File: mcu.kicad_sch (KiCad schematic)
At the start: 59 parts, among them J10 Micro_SD_Card, J11 Conn_01x06, J12 Conn_01x02, J14 USB_B, J8 Conn_02x05_Odd_Even, SW1 SW_Push, SW2 SW_Push, U24 REF3333, U25 LPS25HB, U26 STM32F427ZGTx, U27 USBLC6-2SC6, Y1 8MHz

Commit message: Several optimizations
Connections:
- net DIGITAL5: now reaches U26.66 (PE13)
- net DIGITAL6: now reaches U26.68 (PE15)
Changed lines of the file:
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@@
+    (effects (font (size 1.27 1.27)) (justify right))
+  )
+  (hierarchical_label "DIGITAL6" (shape input) (at 104.14 243.205 180) (fields_autoplaced)
     (effects (font (size 1.27 1.27)) (justify right))
   )
@@
     (effects (font (size 1.27 1.27)) (justify left))
   )
+  (hierarchical_label "DIGITAL5" (shape input) (at 104.14 238.125 180) (fields_autoplaced)
+    (effects (font (size 1.27 1.27)) (justify right))
+  )
   (symbol (lib_id "MCU_ST_STM32F7:STM32F767ZITx") (at 134.62 159.385 0) (unit 1)

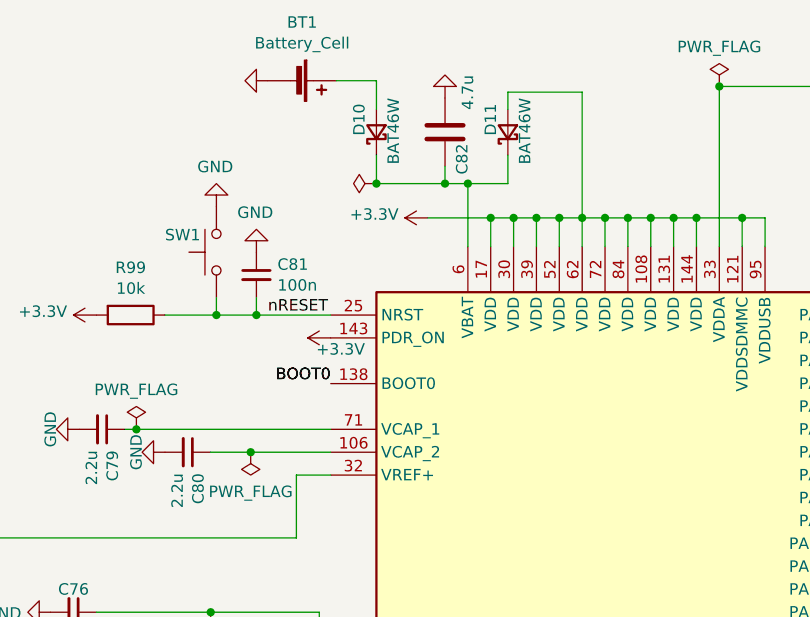
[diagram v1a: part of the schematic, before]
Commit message: Fix connector, optimize psu
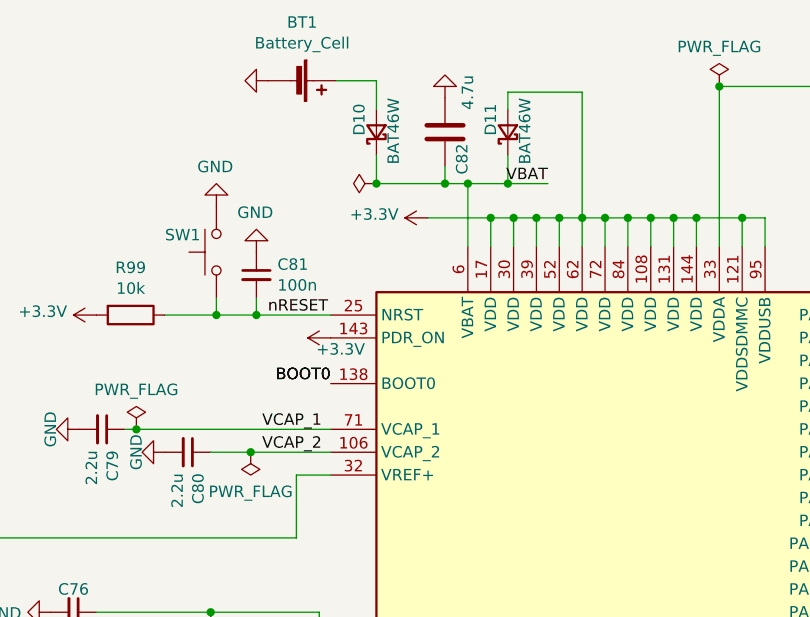
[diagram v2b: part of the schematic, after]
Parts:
- D17: LCSC C8678 -> C15874
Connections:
- net VCAP_2: now reaches C80.1, U26.106 (VCAP_2)
- net VBAT: now reaches C82.1, D10.1 (K), D11.1 (K), U26.6 (VBAT)
- net VCAP_1: now reaches C79.1, U26.71 (VCAP_1)
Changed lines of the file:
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@@
   (junction (at 134.62 252.73) (diameter 0) (color 0 0 0 0)
   )
+  (junction (at 123.825 60.96) (diameter 0) (color 0 0 0 0)
+  )
   (junction (at 65.405 260.35) (diameter 0) (color 0 0 0 0)
   )
@@
     (stroke (width 0) (type default))
   )
+  (wire (pts (xy 123.825 60.96) (xy 128.27 60.96))
+    (stroke (width 0) (type default))
+  )
   (wire (pts (xy 55.245 100.33) (xy 55.245 102.235))
     (stroke (width 0) (type default))
@@
     (effects (font (size 1.27 1.27)) (justify right bottom))
   )
+  (label "VCAP_2" (at 96.52 90.805 0) (fields_autoplaced)
+    (effects (font (size 1.27 1.27)) (justify left bottom))
+  )
   (label "LED3" (at 104.14 217.805 180) (fields_autoplaced)
     (effects (font (size 1.27 1.27)) (justify right bottom))
@@
     (effects (font (size 1.27 1.27)) (justify left bottom))
   )
+  (label "VBAT" (at 128.27 60.96 180) (fields_autoplaced)
+    (effects (font (size 1.27 1.27)) (justify right bottom))
+  )
   (label "AUX_SPI_SCK" (at 81.28 179.705 0) (fields_autoplaced)
     (effects (font (size 1.27 1.27)) (justify left bottom))
@@
     (effects (font (size 1.27 1.27)) (justify right bottom))
   )
+  (label "VCAP_1" (at 96.52 88.265 0) (fields_autoplaced)
+    (effects (font (size 1.27 1.27)) (justify left bottom))
+  )
   (label "AUX_SPI_MISO" (at 292.735 226.695 0) (fields_autoplaced)
     (effects (font (size 1.27 1.27)) (justify left bottom))
@@
       (effects (font (size 1.27 1.27)) hide)
     )
-    (property "LCSC" "C8678" (at 276.225 78.105 0)
+    (property "LCSC" "C15874" (at 276.225 78.105 0)
       (effects (font (size 1.27 1.27)) hide)
     )

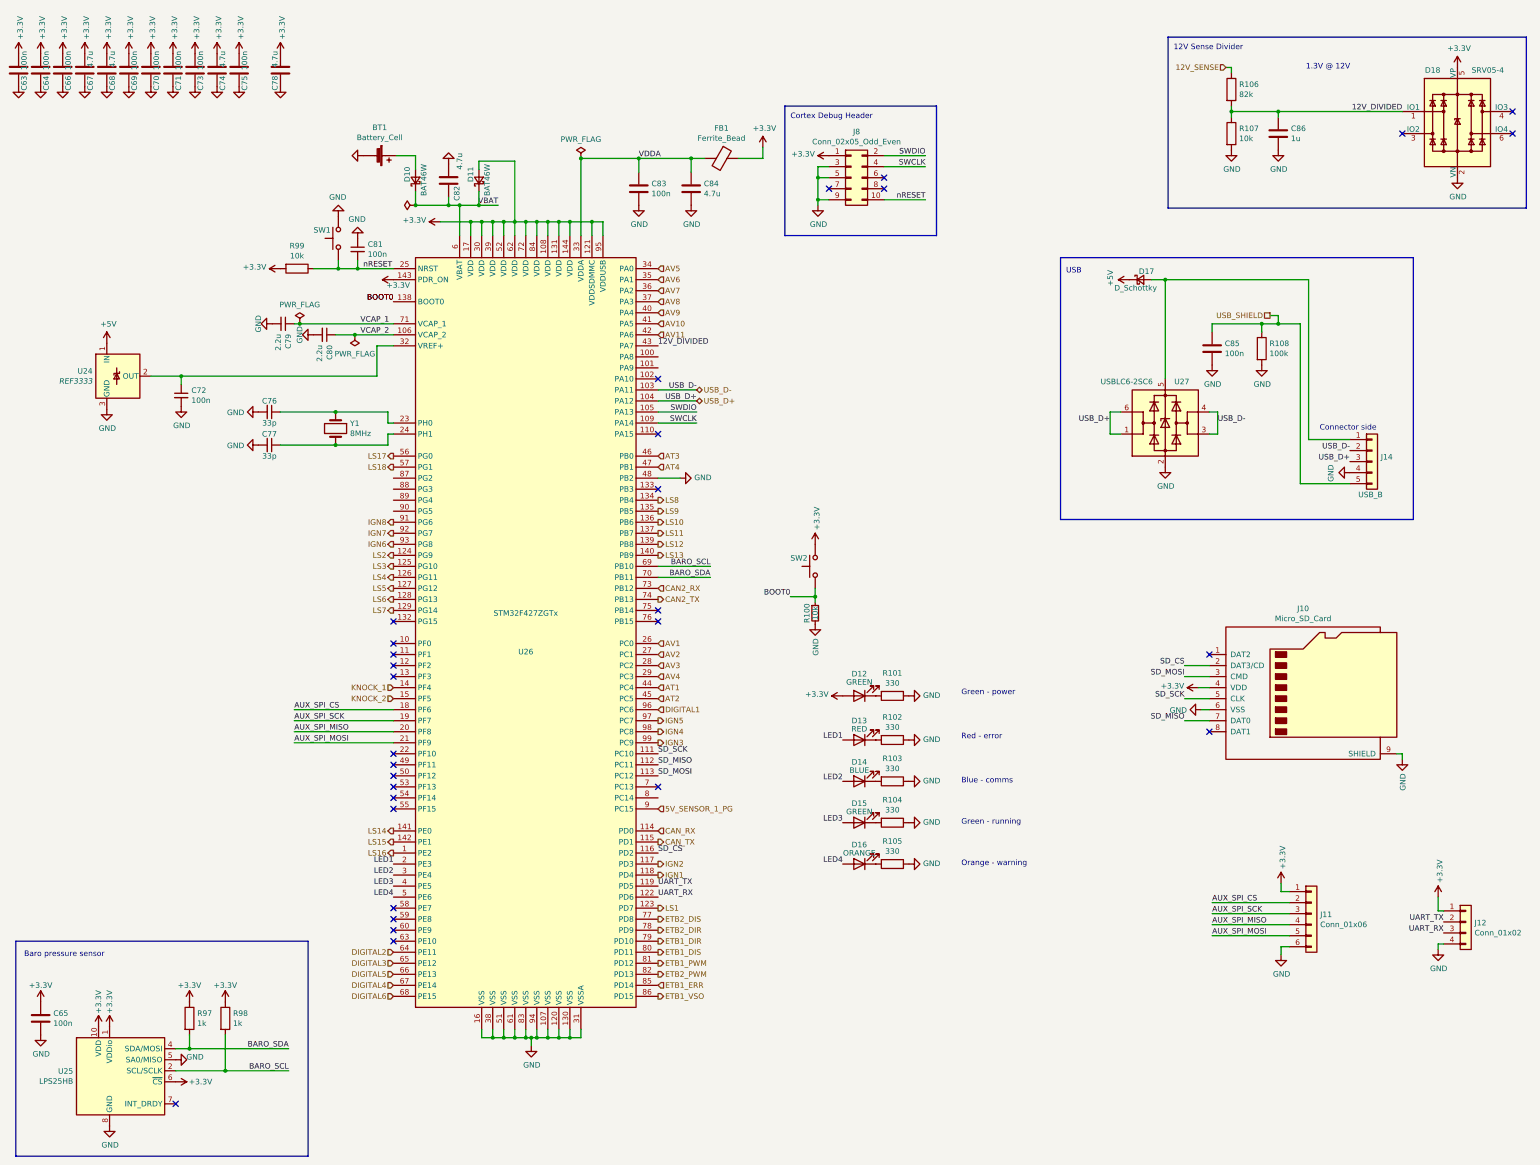
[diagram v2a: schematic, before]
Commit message: Add Stepper, fix Connector, add Testpoints, several changes
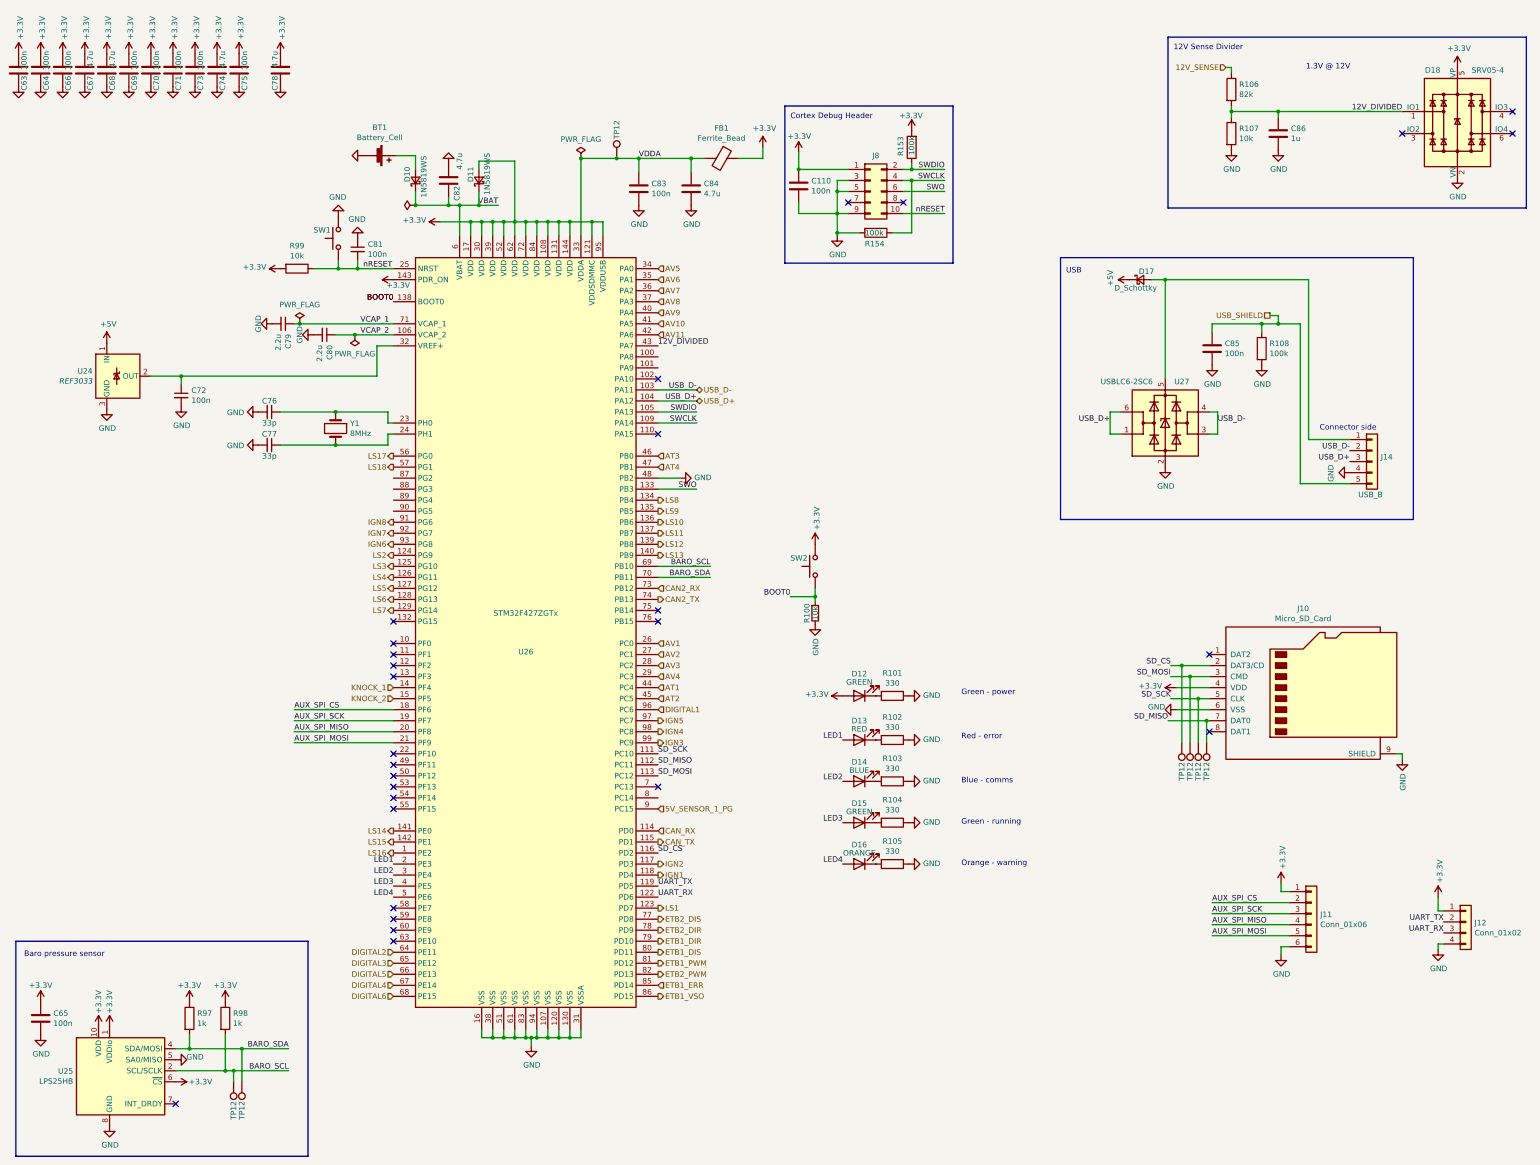
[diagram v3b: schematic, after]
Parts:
- added C110: 100n, Capacitor_SMD:C_0603_1608Metric, symbol Device:C
- added R153, R154: 100k, Resistor_SMD:R_0402_1005Metric, symbol Device:R
- added TP12 (x7): TestPoint, TestPoint:TestPoint_Pad_D1.0mm, symbol Connector:TestPoint
- D10, D11: value BAT46W -> 1N5819WS; footprint Diode_SMD:D_SOD-123 -> Diode_SMD:D_SOD-323; LCSC C83152 -> C191023
- D13: LCSC C84263 -> C2286
- D17: LCSC C15874 -> C14996
- J11, J12, J8: now left out of the parts list
- R97, R98: LCSC C106235 -> C11702
- SW1, SW2: LCSC C318887 -> C318884
- U24: value REF3333 -> REF3033; LCSC C130016 -> C36658; PN REF3033 -> (none)
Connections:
- net +3V3: now also C110.1, R153.2
- net BARO_SCL: now also TP12.1
- net BARO_SDA: now also TP12.1
- net GND: now also C110.2, R154.2
- net SD_CS: now also TP12.1
- net SD_MISO: now also TP12.1
- net SD_MOSI: now also TP12.1
- net SD_SCK: now also TP12.1
- net SWCLK: now also R154.1
- net SWDIO: now also R153.1
- net VDDA: now also TP12.1
- net SWO: now reaches U26.133 (PB3)
- net SWO: now also J8.6 (Pin_6)
- no-connect marks 30 -> 28
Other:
- moved on the sheet: J8

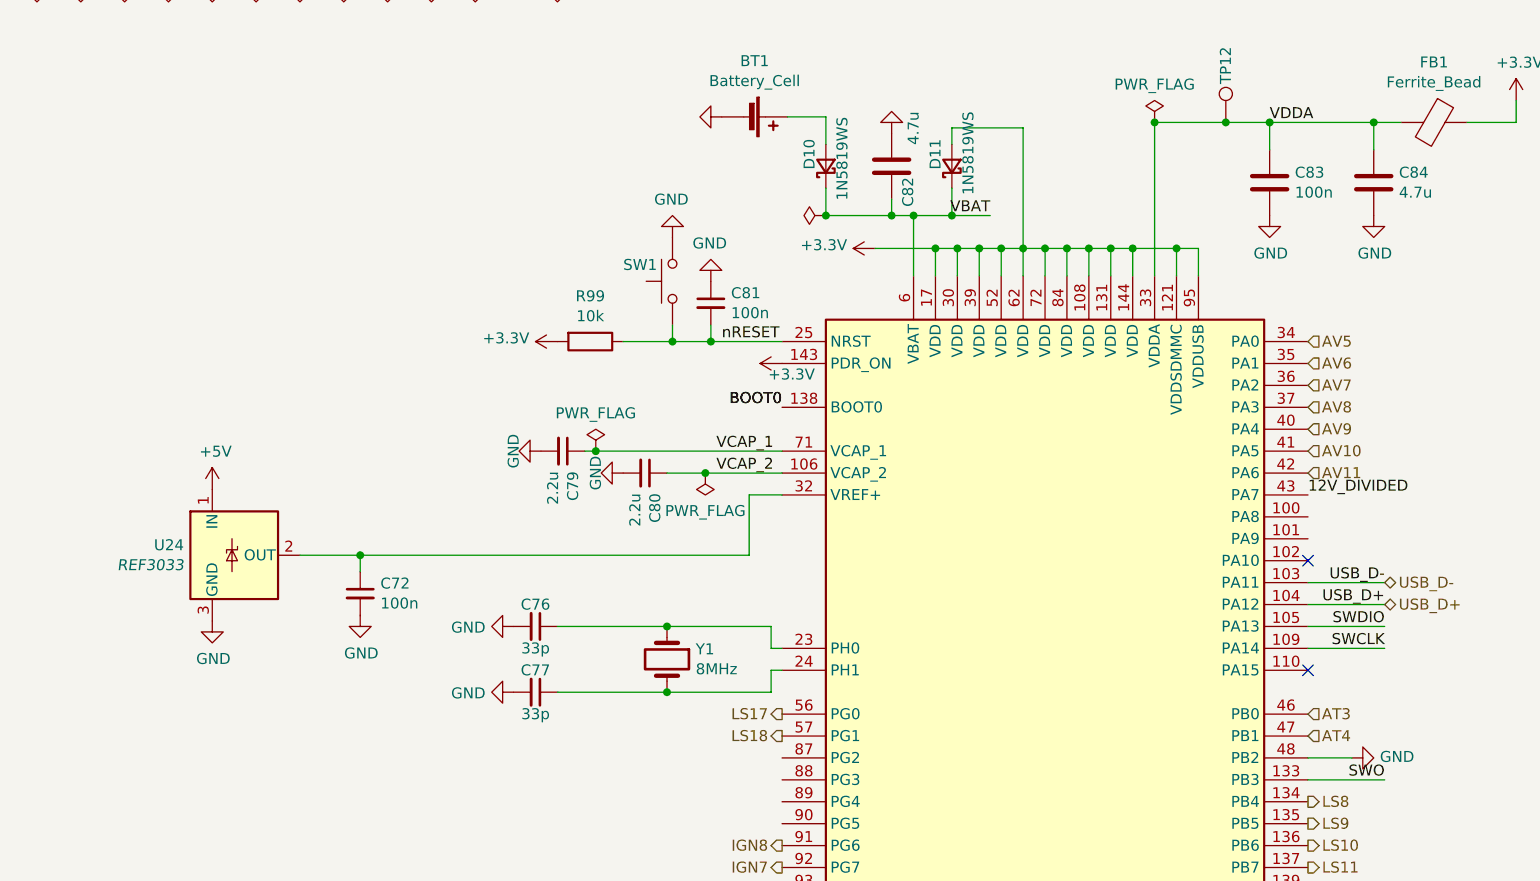
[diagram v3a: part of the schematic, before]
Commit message: Production optimizations, voltage superv, etb sv conn
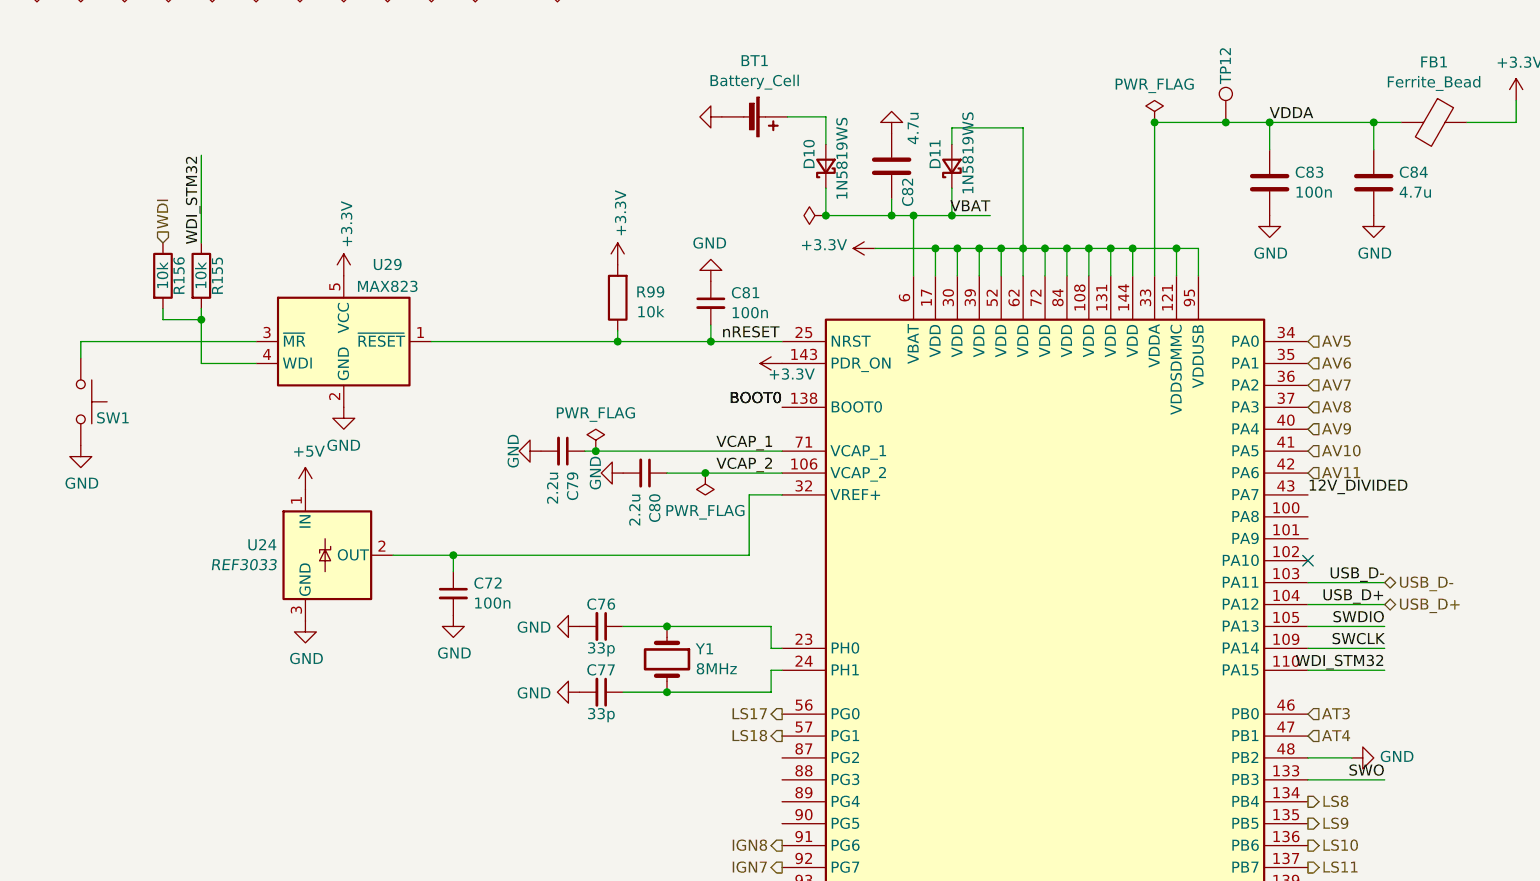
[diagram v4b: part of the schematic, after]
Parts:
- added R155, R156: 10k, Resistor_SMD:R_0402_1005Metric, symbol Device:R
- added U29: MAX823, Package_TO_SOT_SMD:SOT-23-5, symbol MAX823:MAX823
- BT1, J10: JLCRotOffset (none) -> 180
- J14: JLCPosOffset (none) -> -1.27,-2.1
- U27: JLCRotOffset (none) -> 90
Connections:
- net +3V3: now also U29.5 (VCC)
- net GND: now also U29.2 (GND)
- net nRESET: now also U29.1 (~{RESET}); no longer SW1.1
- net WDI_STM32: now reaches U26.110 (PA15)
- net WDI_STM32: now also R155.1
- new net: SW1.1, U29.3 (~{MR})
- new net: R155.2, R156.2, U29.4 (WDI)
- new net WDI: R156.1
- no-connect marks 28 -> 27
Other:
- moved on the sheet: C72, C76, C77, R99, SW1, U24

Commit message: Optimize
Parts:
- added JP5: Jumper_2_Bridged, Jumper:SolderJumper-2_P1.3mm_Open_RoundedPad1.0x1.5mm, symbol Jumper:SolderJumper_2_Open
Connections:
- net ETB1_VSO: now also JP5.1 (A); no longer U26.86 (PD15)
- net SRV05-4-IO2: now reaches D18.3 (IO2)
- new net: JP5.2 (B), U26.86 (PD15)
- no-connect marks 27 -> 26
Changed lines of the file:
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@@
   (no_connect (at 208.915 60.325))
   (no_connect (at 104.14 225.425))
-  (no_connect (at 336.55 44.45))
   (no_connect (at 104.14 194.945))
   (no_connect (at 165.1 100.965))
@@
     (effects (font (size 1.27 1.27)) (justify left))
   )
-  (hierarchical_label "ETB1_VSO" (shape output) (at 165.1 243.205 0) (fields_autoplaced)
+  (hierarchical_label "ETB1_VSO" (shape output) (at 172.72 243.205 0) (fields_autoplaced)
     (effects (font (size 1.27 1.27)) (justify left))
   )
@@
     (effects (font (size 1.27 1.27)) (justify right))
   )
+  (hierarchical_label "SRV05-4-IO2" (shape input) (at 336.55 44.45 180) (fields_autoplaced)
+    (effects (font (size 1.27 1.27)) (justify right))
+  )
   (hierarchical_label "AV9" (shape input) (at 165.1 85.725 0) (fields_autoplaced)
     (effects (font (size 1.27 1.27)) (justify left))
@@
         )
       )
+    )
+  )
+  (symbol (lib_id "Jumper:SolderJumper_2_Open") (at 168.91 243.205 180) (unit 1)
+    (in_bom no) (on_board yes) (dnp no)
+    (property "Reference" "JP5" (at 167.64 245.745 0)
+      (effects (font (size 1.27 1.27)) (justify right))
+    )
+    (property "Value" "Jumper_2_Bridged" (at 170.815 241.3 90)
+      (effects (font (size 1.27 1.27)) (justify right) hide)
+    )
+    (property "Footprint" "Jumper:SolderJumper-2_P1.3mm_Open_RoundedPad1.0x1.5mm" (at 168.91 243.205 0)
+      (effects (font (size 1.27 1.27)) hide)
+    )
+    (property "Datasheet" "~" (at 168.91 243.205 0)
+      (effects (font (size 1.27 1.27)) hide)
+    )
+    (pin "1")
+    (pin "2")
+    (instances
+      (project "proteus"
+        (path "/d9116601-cae2-4199-827b-70fa136aae51"
+          (reference "JP5") (unit 1)
+        )
+        (path "/d9116601-cae2-4199-827b-70fa136aae51/03d0e383-f766-4dec-ae30-e02bba269810"
+          (reference "JP13") (unit 1)
+        )
+        (path "/d9116601-cae2-4199-827b-70fa136aae51/00000000-0000-0000-0000-00005d99e6ee"
+          (reference "JP1") (unit 1)
+        )
+      )
